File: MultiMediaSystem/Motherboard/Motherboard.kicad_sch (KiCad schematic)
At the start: 43 parts, among them J1 Wire Harness, J10 RF_EN, J14 5V_1, J15 RPI_Buck, J16 AUSB2-4599, J17 Illum/Dim, J18 5V_2, J19 GP_Buck, J2 Vmem Jumper, J20 5V_3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

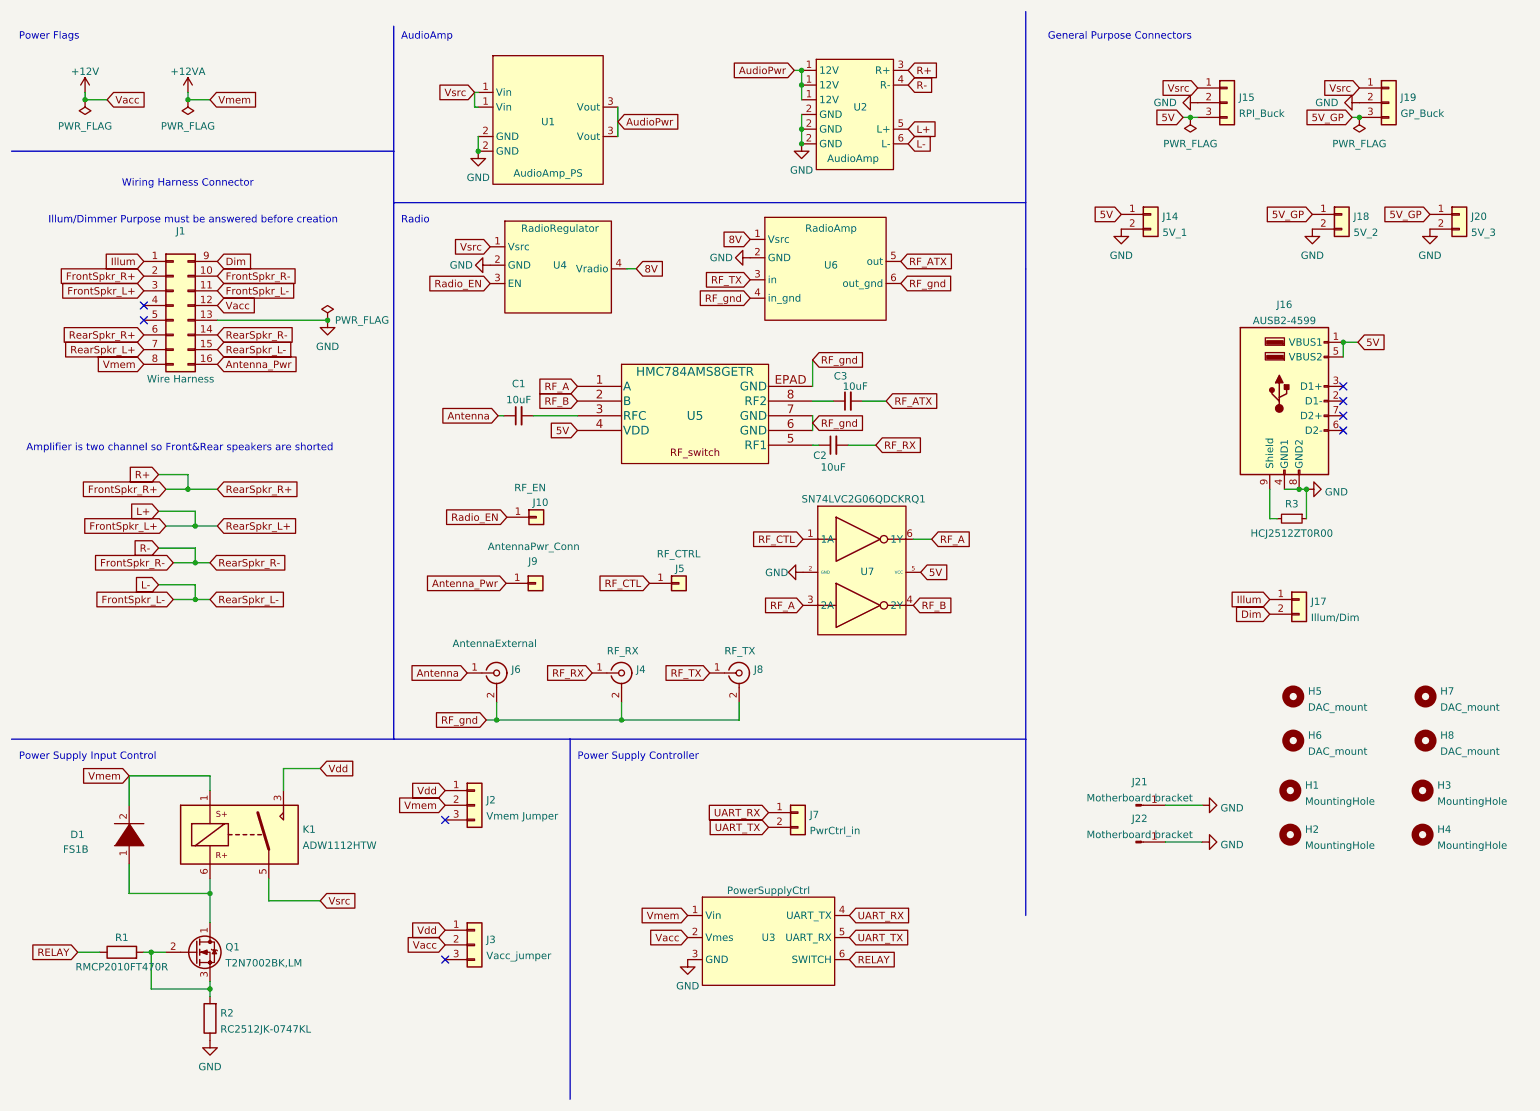
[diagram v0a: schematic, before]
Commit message: Adjusted Motherboard Pinouts
Motherboard pinout's were slightly off. This corrects that problem.
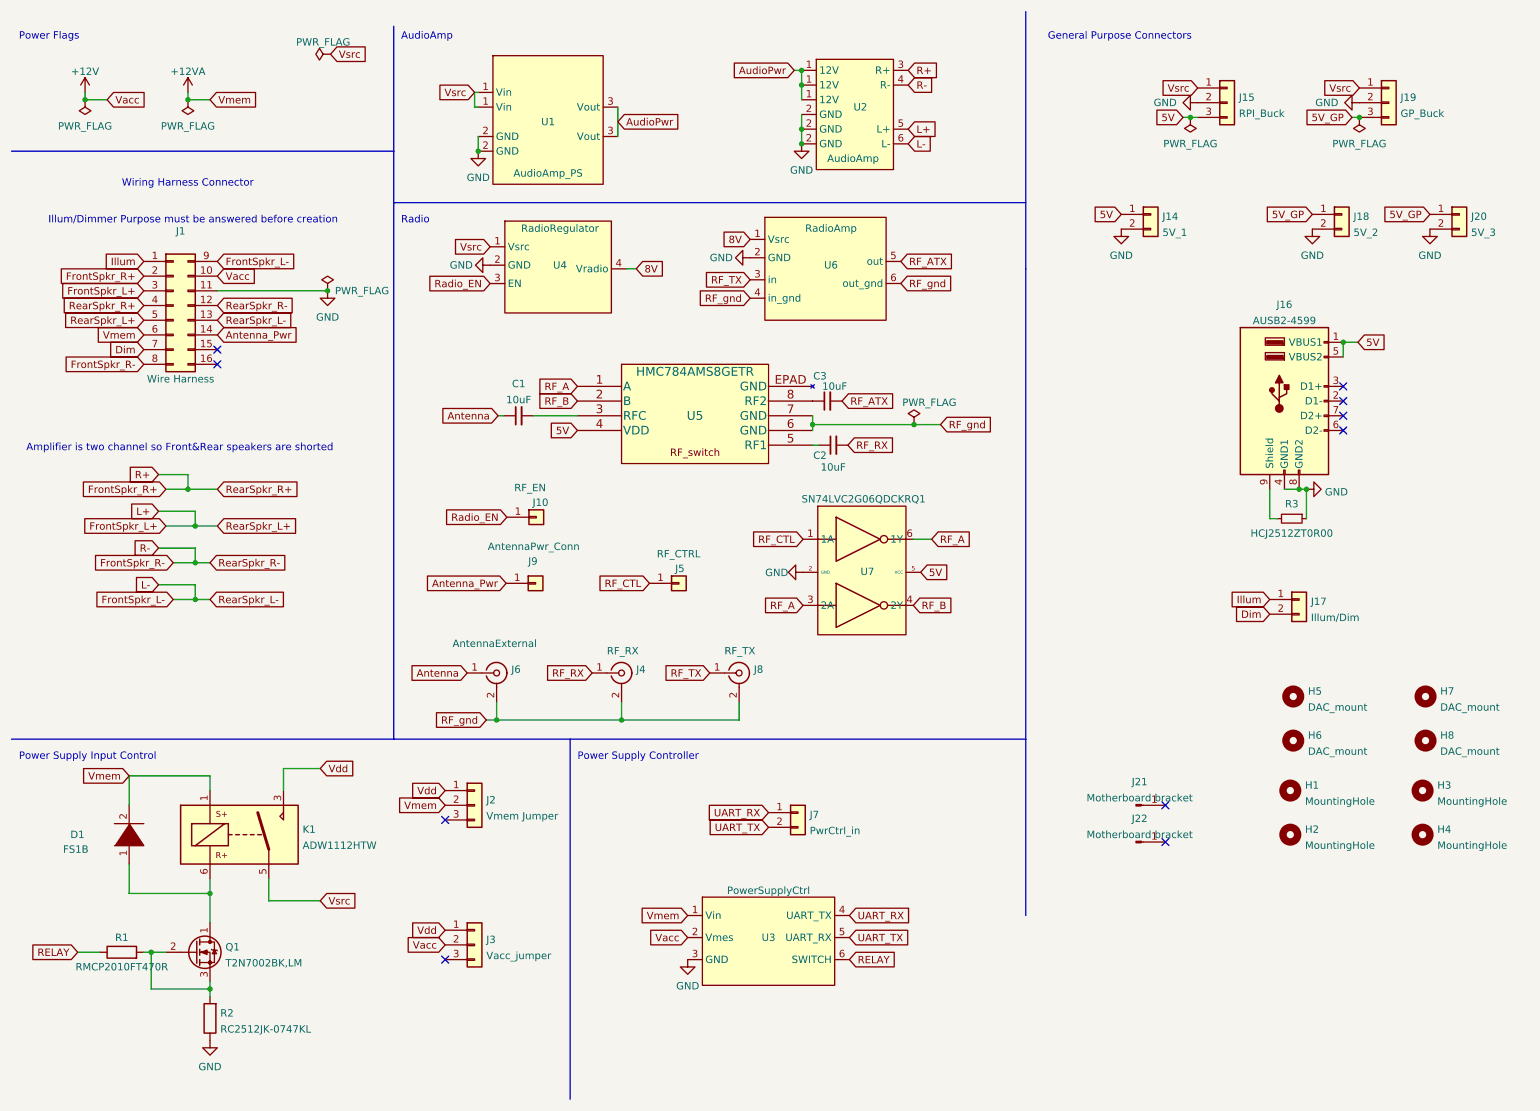
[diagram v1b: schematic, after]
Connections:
- net +12V: now also J1.10 (Pin_10); no longer J1.12 (Pin_12)
- net +12VA: now also J1.6 (Pin_6); no longer J1.8 (Pin_8)
- net Antenna_Pwr: now also J1.14 (Pin_14); no longer J1.16 (Pin_16)
- net Dim: now also J1.7 (Pin_7); no longer J1.9 (Pin_9)
- net FrontSpkr_L+: now also J1.5 (Pin_5); no longer J1.7 (Pin_7)
- net FrontSpkr_L-: now also J1.13 (Pin_13), J1.9 (Pin_9); no longer J1.11 (Pin_11), J1.15 (Pin_15)
- net FrontSpkr_R+: now also J1.4 (Pin_4); no longer J1.6 (Pin_6)
- net FrontSpkr_R-: now also J1.12 (Pin_12), J1.8 (Pin_8); no longer J1.10 (Pin_10), J1.14 (Pin_14)
- net GND: now also J1.11 (Pin_11); no longer J1.13 (Pin_13), J21.1 (Pin_1), J22.1 (Pin_1)
- net RF_gnd: no longer U5.EPAD (GND)
- no-connect marks 8 -> 10
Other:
- moved on the sheet: C3

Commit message: Updated all designs
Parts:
- removed J7: PwrCtrl_in, Connector_PinSocket_2.54mm:PinSocket_1x02_P2.54mm_Vertical, symbol Connector_Generic:Conn_01x02
- J15, J19: footprint Connector_PinSocket_2.54mm:PinSocket_1x03_P2.54mm_Vertical -> Custom:5V_Reg_Footprint_VertMnt
- Q1: footprint Package_TO_SOT_SMD:SOT-23 -> Custom:SOT-23
- R1: value RMCP2010FT470R -> 470 Ohm
- R2: value RC2512JK-0747KL -> 47K
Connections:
- net 5V: no longer J16.1 (VBUS1), J16.5 (VBUS2), U5.4 (VDD), U7.5 (VCC)
- net 5V_GP: now also J16.1 (VBUS1), J16.5 (VBUS2), U5.4 (VDD), U7.5 (VCC)
- net GND: now also Q1.3 (S)
- net at Q1.2 (G), R1.2, R2.2: no longer Q1.3 (S)
- net UART_RX: no longer names the net of U3.4 (UART_TX)
- net UART_TX: no longer names the net of U3.5 (UART_RX)
- no-connect marks 10 -> 12
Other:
- moved on the sheet: R2
